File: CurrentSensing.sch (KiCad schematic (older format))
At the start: 7 parts

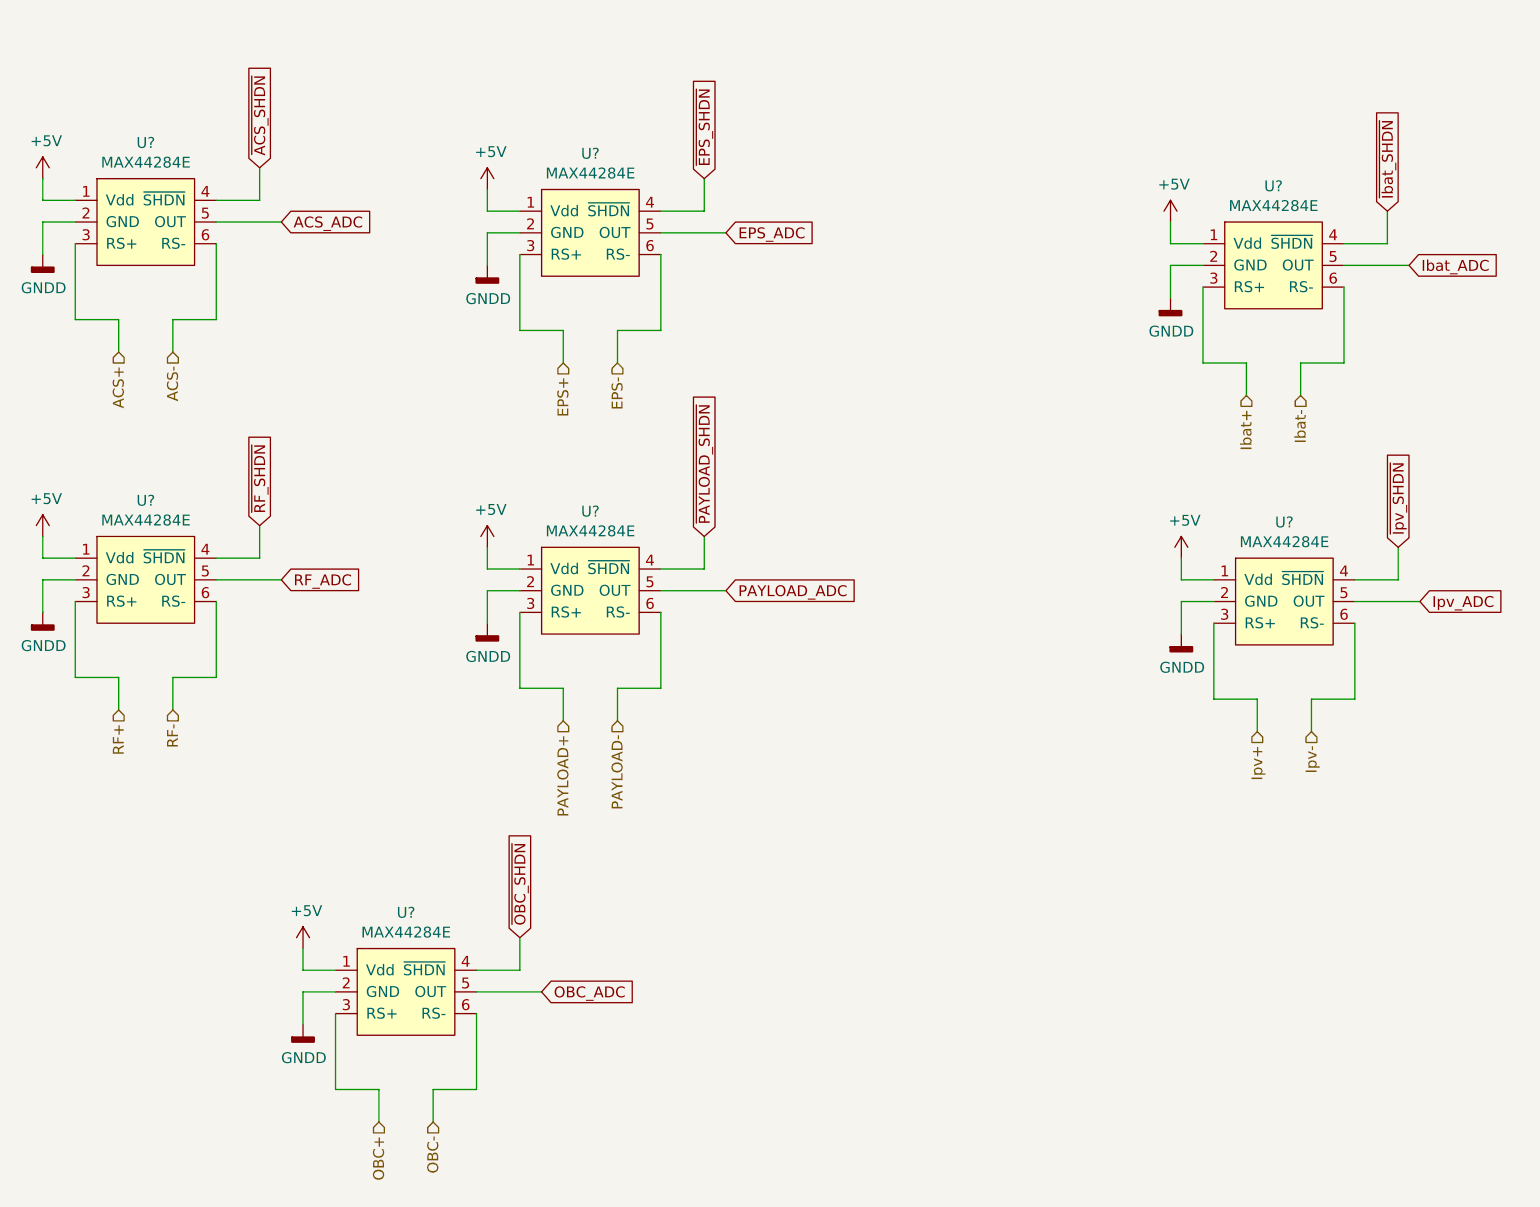
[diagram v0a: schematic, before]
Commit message: updated PDU schematic with footprints
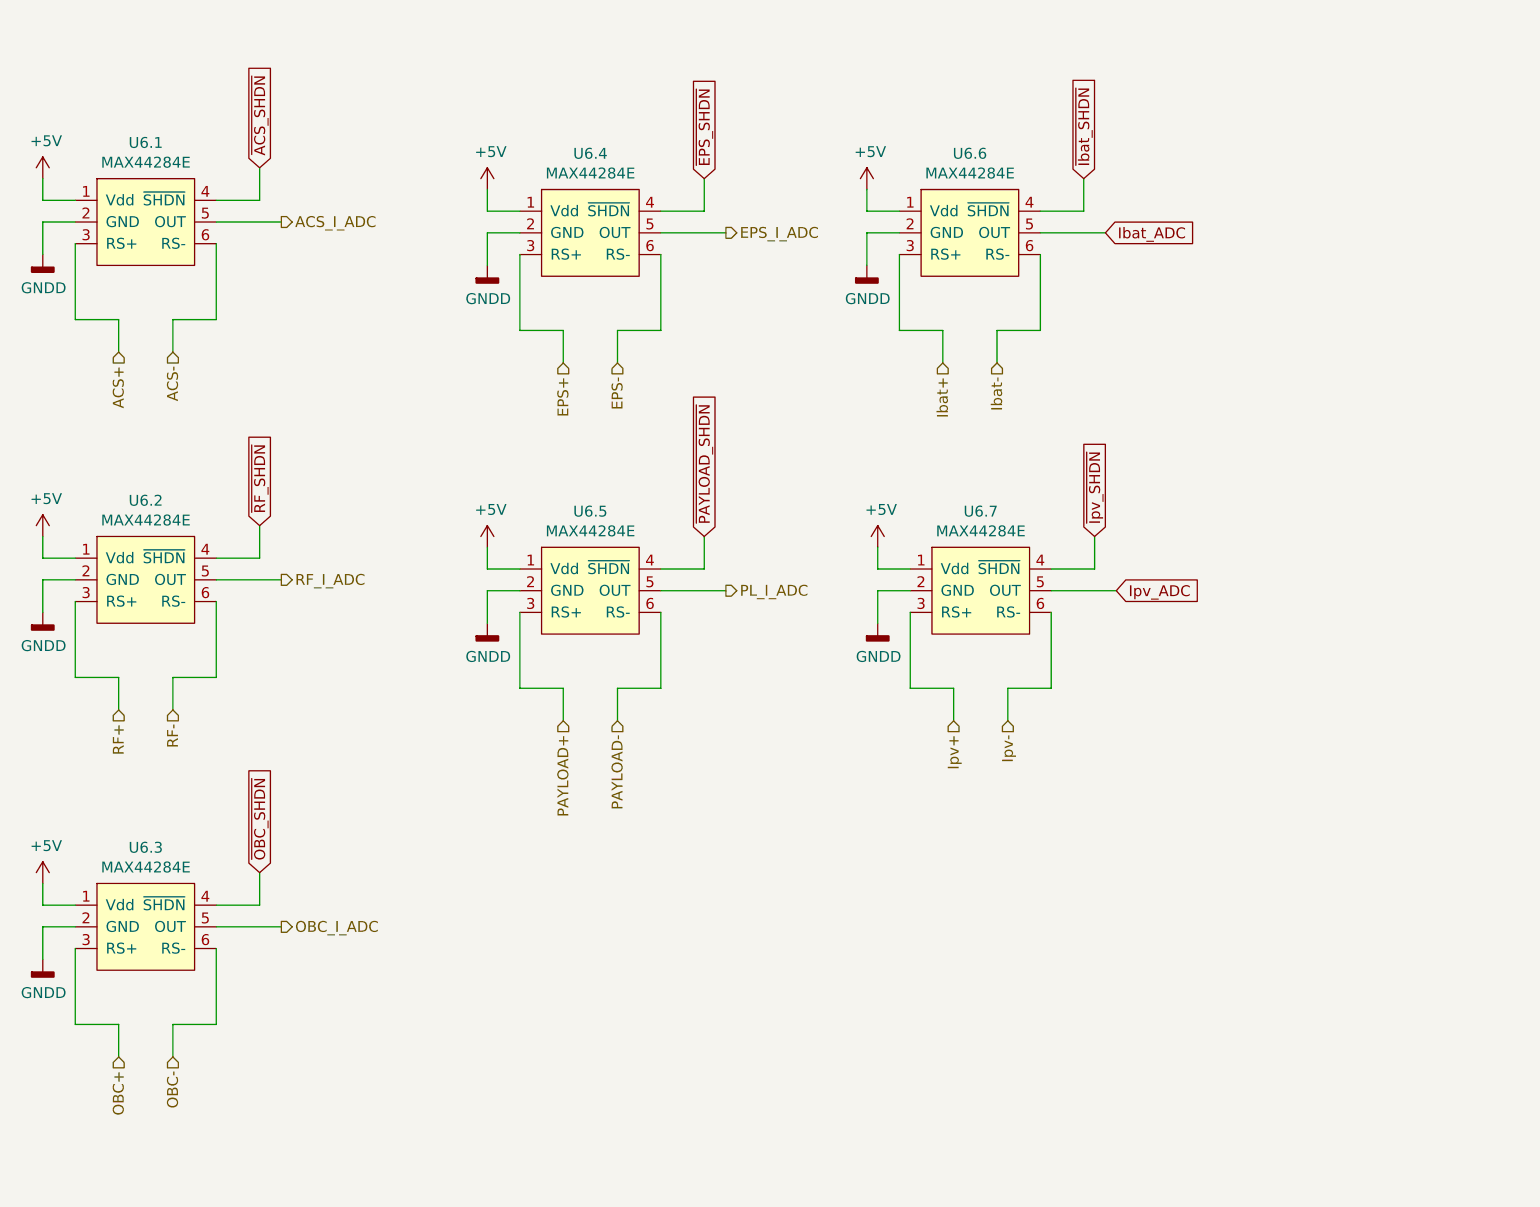
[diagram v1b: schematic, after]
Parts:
- U6.1, U6.3, U6.4, U6.6, U6.7: renamed from U?; footprint (none) -> Package_TO_SOT_SMD:SOT-23-6
- U6.2, U6.5: renamed from U?; footprint (none) -> Package_TO_SOT_SMD:SOT-23-8
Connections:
- net ACS_ADC renamed ACS_I_ADC
- net EPS_ADC renamed EPS_I_ADC
- net OBC_ADC renamed OBC_I_ADC
- net PAYLOAD_ADC renamed PL_I_ADC
- net RF_ADC renamed RF_I_ADC
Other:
- moved on the sheet: U6.3, U6.6, U6.7
